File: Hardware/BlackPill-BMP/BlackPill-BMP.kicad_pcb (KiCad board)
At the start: 2 copper layers, 72.4 x 60 mm, 39 parts, among them J1 JTAG, J2 VCC, J3 GND, J4 SWO, J5 GDB_COMM, J6 TVCC, J7 LogicAna, J8 Conn_01x10, J9 Conn_01x11, U1 BlueAndBlackPill, U2 AD8531ARTZ, U3 SRV05-4, U4 TXS0108EPW, U5 SRV05-4

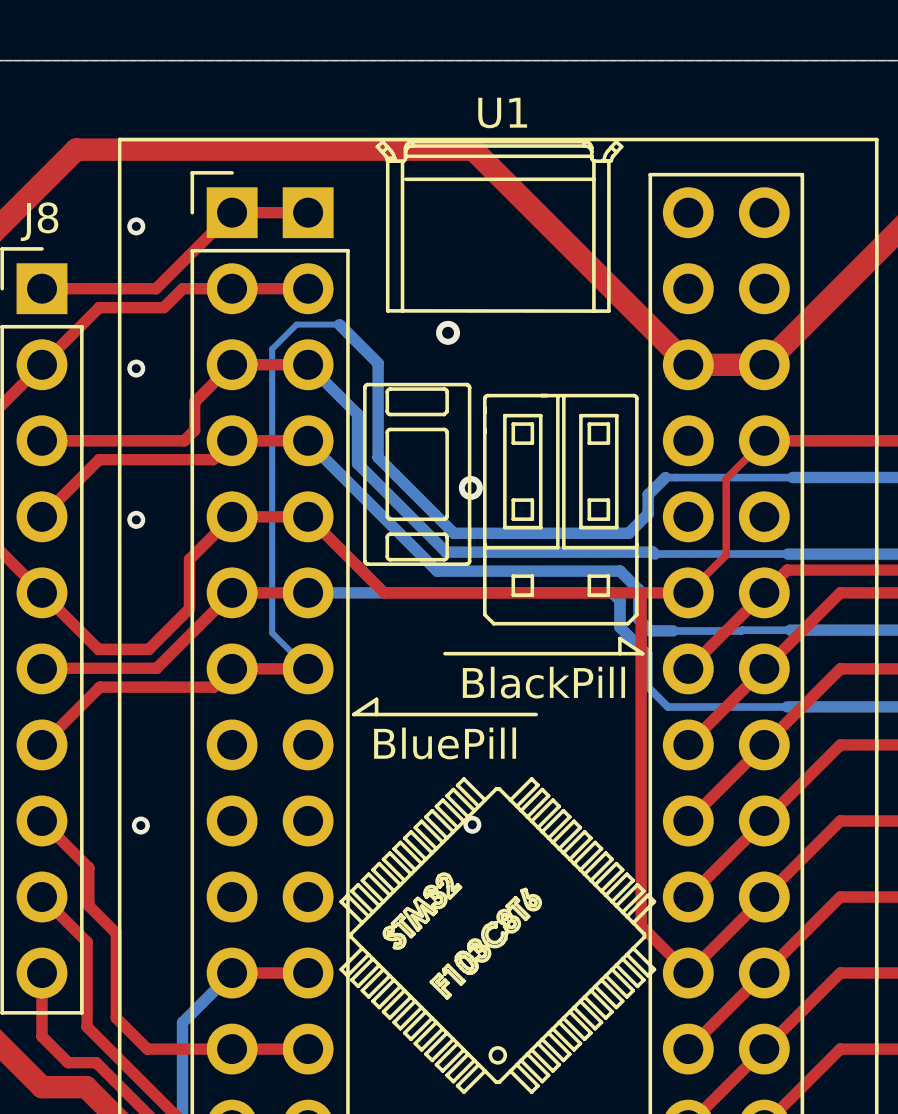
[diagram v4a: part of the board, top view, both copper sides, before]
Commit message: Files for PCB Manufacturing of 4 boards. Preparation for Board documentation
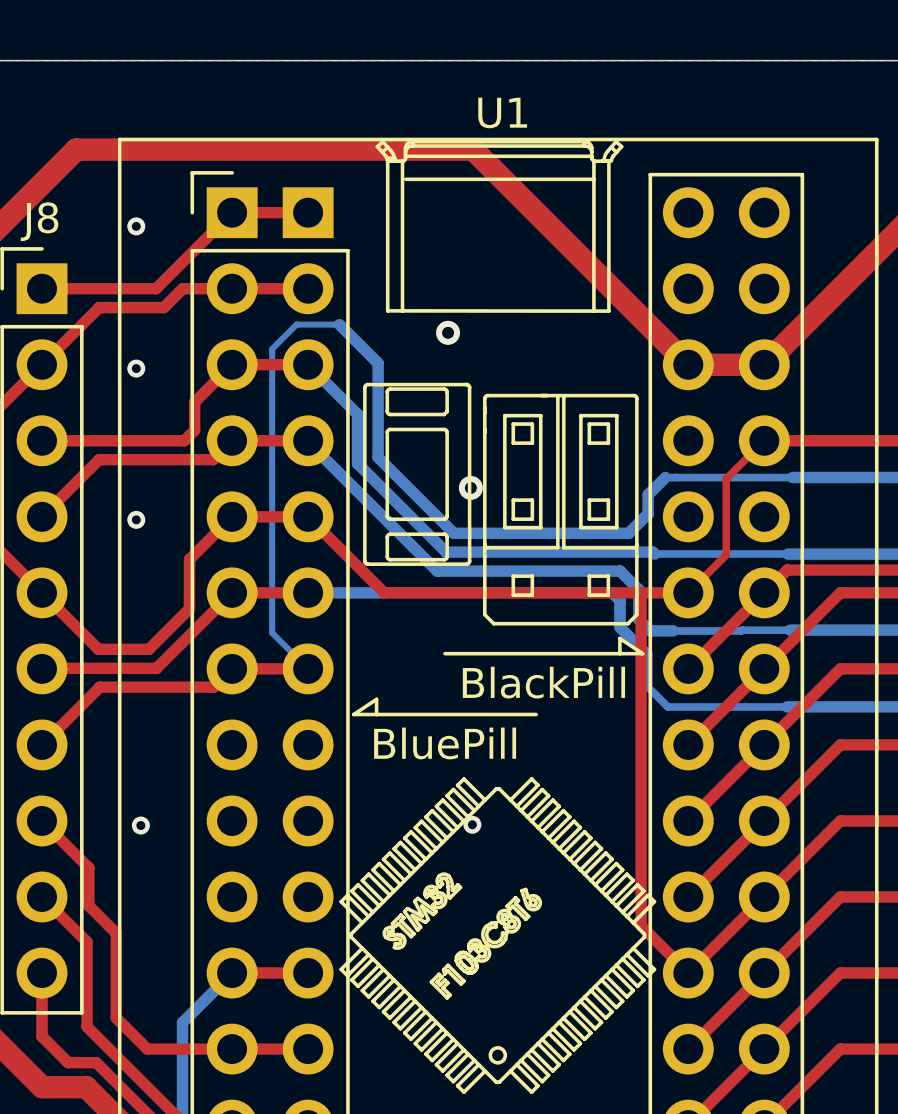
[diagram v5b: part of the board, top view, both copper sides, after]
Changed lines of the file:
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@@
     (fp_arc (start 9.164109 23.475359) (mid 9.19312 23.534447) (end 9.169421 23.59583) (layer "F.SilkS") (width 0.12))
     (fp_arc (start 7.057769 23.137421) (mid 6.881082 23.21257) (end 6.704534 23.137103) (layer "F.SilkS") (width 0.12))
-    (fp_arc (start 5.238052 24.032461) (mid 5.300519 24.004429) (end 5.368722 24.010576) (layer "F.SilkS") (width 0.12))
+    (fp_arc (start 5.238052 24.032461) (mid 5.300525 24.004403) (end 5.368722 24.010576) (layer "F.SilkS") (width 0.12))
     (fp_arc (start 6.919342 22.160794) (mid 7.078414 22.093934) (end 7.23752 22.160688) (layer "F.SilkS") (width 0.12))
     (fp_arc (start 5.698 35.022588) (mid 3.648 32.972588) (end 5.698 30.922588) (layer "F.SilkS") (width 0.12))
@@
     (fp_arc (start 4.534 11.742) (mid 4.463289 11.712711) (end 4.434 11.642) (layer "F.SilkS") (width 0.12))
     (fp_arc (start 5.153056 37.032958) (mid 5.435907 37.150103) (end 5.553056 37.432958) (layer "F.SilkS") (width 0.12))
-    (fp_arc (start 5.139252 24.209874) (mid 5.084094 24.072059) (end 5.143927 23.93621) (layer "F.SilkS") (width 0.12))
+    (fp_arc (start 5.139252 24.209874) (mid 5.084089 24.072059) (end 5.143927 23.93621) (layer "F.SilkS") (width 0.12))
     (fp_arc (start 9.317515 23.529327) (mid 9.430619 23.534642) (end 9.527224 23.593706) (layer "F.SilkS") (width 0.12))
     (fp_arc (start 5.459023 24.262355) (mid 5.542039 24.256717) (end 5.62082 24.283496) (layer "F.SilkS") (width 0.12))
-    (fp_arc (start 8.952381 23.377727) (mid 9.10311 23.311203) (end 9.254729 23.375603) (layer "F.SilkS") (width 0.12))
+    (fp_arc (start 8.952381 23.377727) (mid 9.10311 23.311139) (end 9.254729 23.375603) (layer "F.SilkS") (width 0.12))
     (fp_arc (start 11.765 -2.226605) (mid 11.931822 -2.175277) (end 12.014999 -2.021817) (layer "F.SilkS") (width 0.12))
     (fp_arc (start 5.284 6.742) (mid 5.213289 6.712711) (end 5.184 6.642) (layer "F.SilkS") (width 0.12))
@@
     (fp_arc (start 8.035776 25.146132) (mid 8.038453 25.196504) (end 8.014105 25.240682) (layer "F.SilkS") (width 0.12))
     (fp_arc (start 10.130326 23.124461) (mid 10.057435 23.149835) (end 9.98797 23.116175) (layer "F.SilkS") (width 0.12))
-    (fp_arc (start 4.96647 38.715042) (mid 4.943912 38.616314) (end 4.944082 38.515042) (layer "F.SilkS") (width 0.12))
+    (fp_arc (start 4.96647 38.715042) (mid 4.943897 38.616315) (end 4.944082 38.515042) (layer "F.SilkS") (width 0.12))
     (fp_arc (start 5.131166 -1.890847) (mid 5.176978 -1.815287) (end 5.193572 -1.7285) (layer "F.SilkS") (width 0.12))
     (fp_arc (start 8.519575 24.925586) (mid 8.342887 25.00072) (end 8.166341 24.925267) (layer "F.SilkS") (width 0.12))
@@
     (fp_arc (start 7.23752 22.160688) (mid 7.328273 22.324575) (end 7.354273 22.510098) (layer "F.SilkS") (width 0.12))
     (fp_arc (start 12.859998 39.524619) (mid 12.830711 39.594711) (end 12.760619 39.623998) (layer "F.SilkS") (width 0.12))
-    (fp_arc (start 5.315142 -2.054759) (mid 5.407732 -1.900877) (end 5.439988 -1.724215) (layer "F.SilkS") (width 0.12))
+    (fp_arc (start 5.315142 -2.054759) (mid 5.407707 -1.900875) (end 5.439988 -1.724215) (layer "F.SilkS") (width 0.12))
     (fp_arc (start 8.441283 6.21) (mid 8.470571 6.139283) (end 8.541283 6.11) (layer "F.SilkS") (width 0.12))
     (fp_arc (start 9.265884 23.689744) (mid 9.344175 23.652102) (end 9.425556 23.682413) (layer "F.SilkS") (width 0.12))
@@
       (net 55 "unconnected-(U1-PadB40)") (pinfunction "5V") (pintype "power_in+no_connect"))
     (model "${KIPRJMOD}/lib/blackpill v2.0.step"
-      (offset (xyz 10 -25 5.5))
+      (offset (xyz 10 -25 10))
       (scale (xyz 1 1 1))
       (rotate (xyz 0 0 90))
     )
     (model "${KICAD6_3DMODEL_DIR}/Connector_PinHeader_2.54mm.3dshapes/PinHeader_1x20_P2.54mm_Vertical.wrl"
-      (offset (xyz 2.5 0 5.5))
+      (offset (xyz 2.5 0 10))
       (scale (xyz 1 1 1))
       (rotate (xyz 0 180 0))
     )
     (model "${KICAD6_3DMODEL_DIR}/Connector_PinHeader_2.54mm.3dshapes/PinHeader_1x20_P2.54mm_Vertical.wrl"
-      (offset (xyz 17.6 0 5.5))
+      (offset (xyz 17.6 0 10))
       (scale (xyz 1 1 1))
       (rotate (xyz 0 -180 0))
     )
+    (model "${KICAD6_3DMODEL_DIR}/Connector_PinSocket_2.54mm.3dshapes/PinSocket_2x20_P2.54mm_Vertical.wrl"
+      (offset (xyz 2.5 0 0))
+      (scale (xyz 1 1 1))
+      (rotate (xyz 0 0 0))
+    )
+    (model "${KICAD6_3DMODEL_DIR}/Connector_PinSocket_2.54mm.3dshapes/PinSocket_2x20_P2.54mm_Vertical.wrl"
+      (offset (xyz 17.8 0 0))
+      (scale (xyz 1 1 1))
+      (rotate (xyz 0 0 0))
+    )
+    (model "P:/github.com/glossy-msp430/Hardware/BluePill-BMP/lib/YAAJ_BluePill_PinHeaders_H_SWD_cp.wrl" hide
+      (offset (xyz 0 0 7.5))
+      (scale (xyz 1 1 1))
+      (rotate (xyz 0 0 0))
+    )
   )

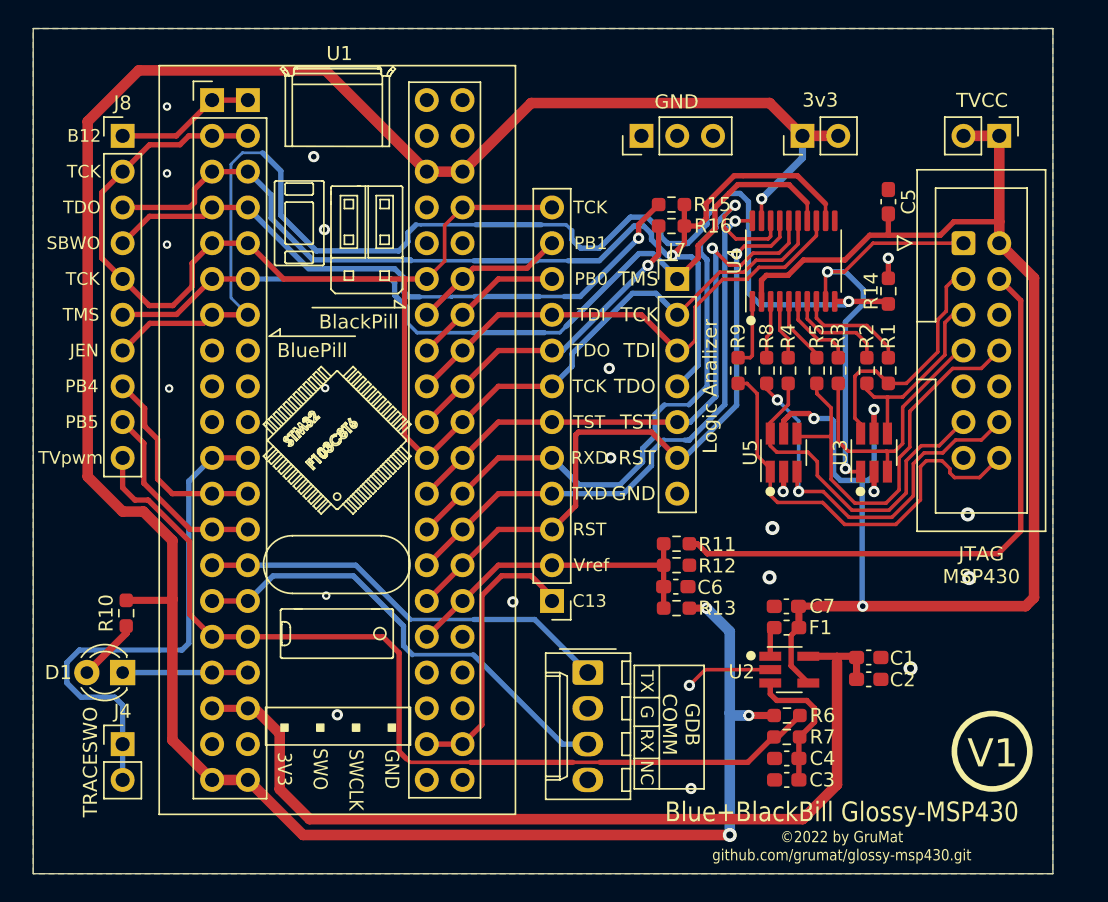
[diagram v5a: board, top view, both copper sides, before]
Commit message: Swapped LRXD and LTXD on both prototype boards.
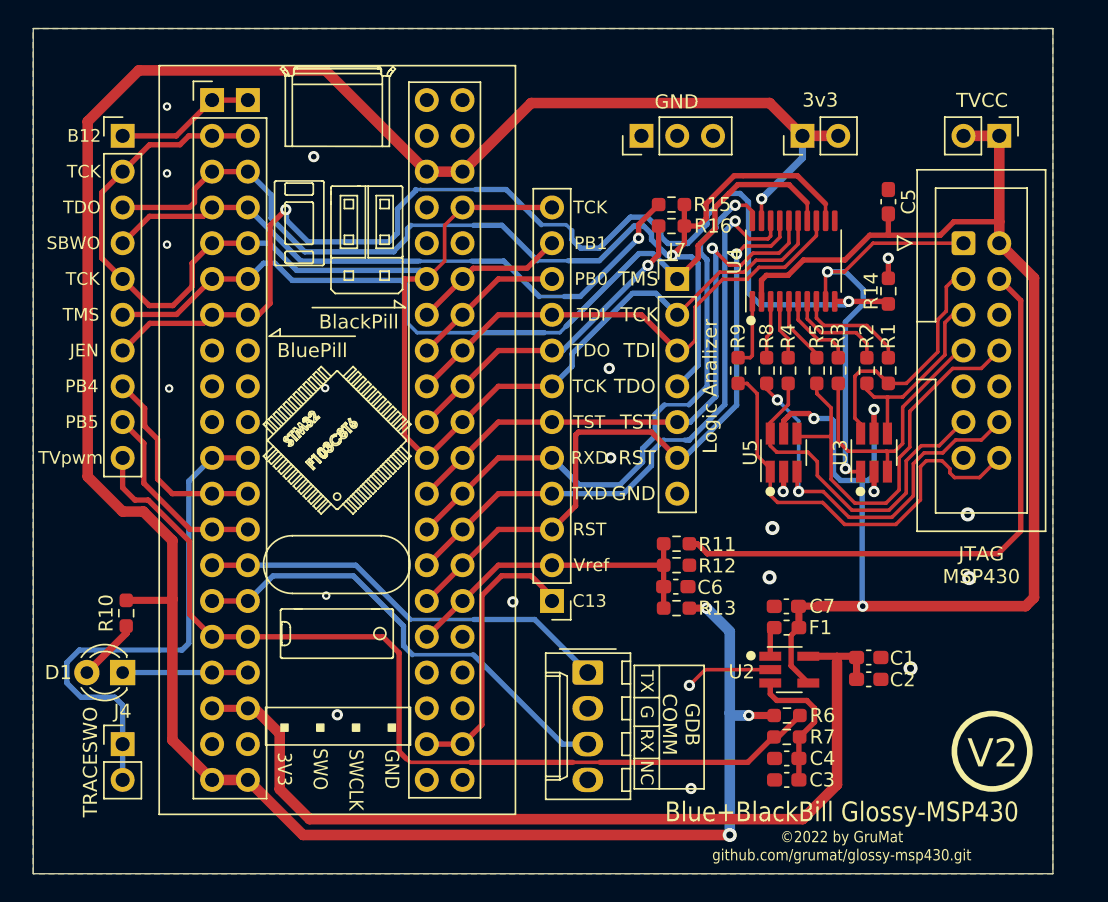
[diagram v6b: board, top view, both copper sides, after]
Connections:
- R8 pad 1: /LRXD -> /LTXD
- R9 pad 1: /LTXD -> /LRXD
- U4 pad 1: /LTXD -> /LRXD
- U4 pad 18: /mRXD -> /mTXD
- U4 pad 20: /mTXD -> /mRXD
- U4 pad 3: /LRXD -> /LTXD
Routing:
- net /JENA: track 87.1 -> 79.8 mm, vias 1 -> 2
- net /mRXD: track 50.8 -> 46.2 mm
- net /mTXD: track 41.0 -> 44.2 mm
- net /LTDO: track 75.8 -> 77.8 mm
- net /mTCK: track 106.9 -> 108.6 mm
- net /mTMS: track 68.8 -> 70.1 mm
- net /LTXD: track 4.92 -> 4.11 mm
- net /LRXD: track 4.11 -> 4.92 mm
- net /SBWO: track 45.6 -> 45.0 mm
- net GND: vias 22 -> 21
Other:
- board text added: "V2"
- board text removed: "V1"

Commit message: Review of ESD protection for Development boards.
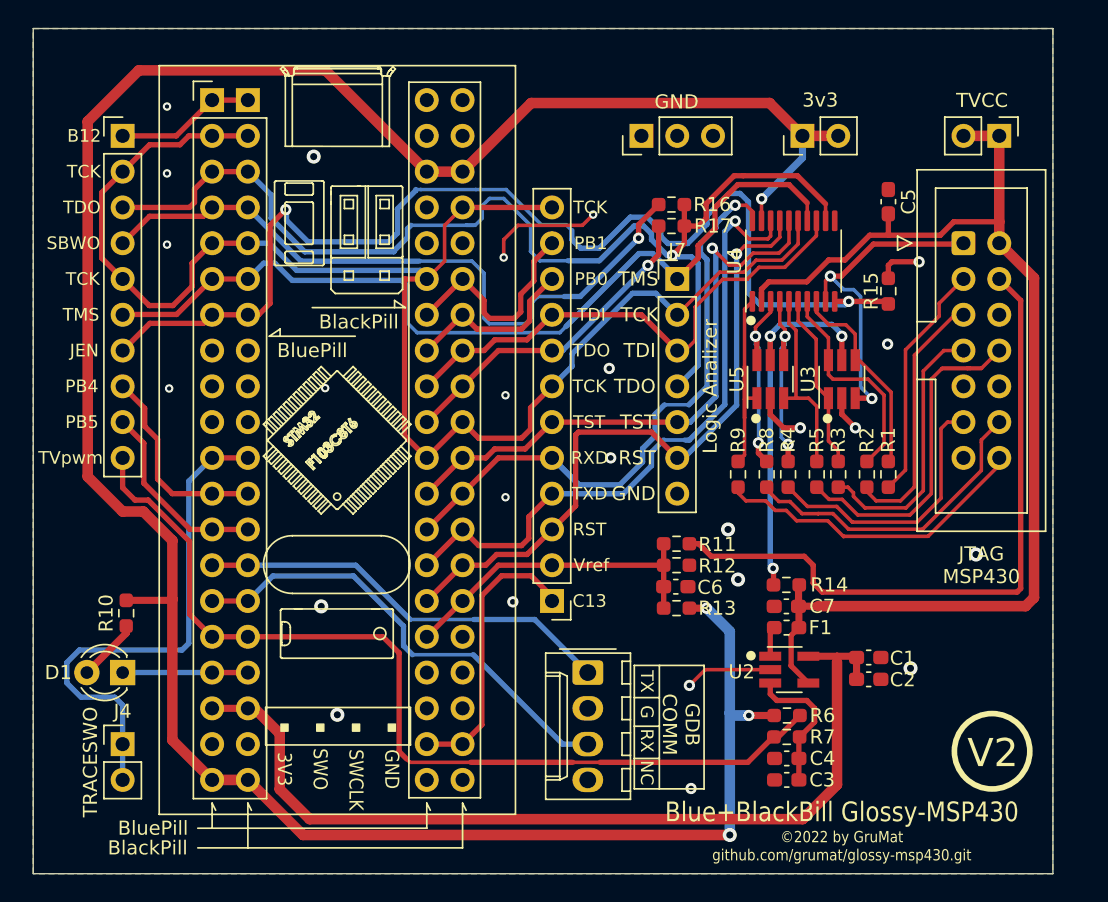
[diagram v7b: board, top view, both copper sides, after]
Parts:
- added R14: 10K, Resistor_SMD:R_0603_1608Metric_Pad0.98x0.95mm_HandSolder, F.Cu at (170.3, 104.5)
- R8, R9: value 100 -> 330
- moved R1 7.37 mm to (177.5, 96.6)
- moved R2 7.37 mm to (176.0, 96.6)
- moved R3 7.37 mm to (174.0, 96.6)
- moved R4 7.37 mm to (170.4, 96.6)
- moved R5 7.37 mm to (172.5, 96.6)
- moved R8 7.37 mm to (168.9, 96.6)
- moved R9 7.37 mm to (166.9, 96.6)
- moved U3 5.69 mm to (174.2, 89.9)
- moved U5 5.30 mm to (169.2, 89.9)
- renumbered R14 to R15, R15 to R16, R16 to R17
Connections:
- U3 pad 1: /JTDO -> /LTCK
- U3 pad 3: /JTCK -> /JTDO
- U3 pad 4: /JTMS -> /LTDI
- U3 pad 5: /TVCC -> Net-(R14-Pad2)
- U3 pad 6: /JTDI -> /LTMS
- U5 pad 1: /JRXD -> /LRXD
- U5 pad 3: /JTXD -> /LTEST
- U5 pad 4: /JTEST -> /LRST
- U5 pad 5: /TVCC -> Net-(R14-Pad2)
- U5 pad 6: /JRST -> /LTXD
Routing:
- net Net-(R14-Pad2): track 0.00 -> 27.1 mm, vias 0 -> 3
- net /TVCC: track 108.3 -> 82.3 mm, vias 3 -> 0
- net GND: track 10.5 -> 24.0 mm, vias 21 -> 25
- net /LRXD: track 4.92 -> 16.3 mm
- net /LTXD: track 4.11 -> 13.9 mm, vias 0 -> 2
- net /LRST: track 4.24 -> 13.6 mm, vias 0 -> 2
- net /LTEST: track 4.81 -> 13.6 mm
- net /LTMS: track 7.21 -> 15.6 mm
- net /JRXD: track 30.9 -> 22.9 mm
- net /JTXD: track 29.2 -> 22.2 mm, vias 2 -> 0
- net /LTCK: track 5.71 -> 12.5 mm
- net /LTDI: track 7.90 -> 14.5 mm
- net /JTDO: track 30.1 -> 23.9 mm
- net /JRST: track 25.1 -> 19.3 mm
- net /TVref: track 43.0 -> 48.4 mm
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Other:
- board text added: "BlackPill"
- board text added: "BluePill"

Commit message: Swap mTMS and JENA pins for optimized DMA use in BluePill variant.
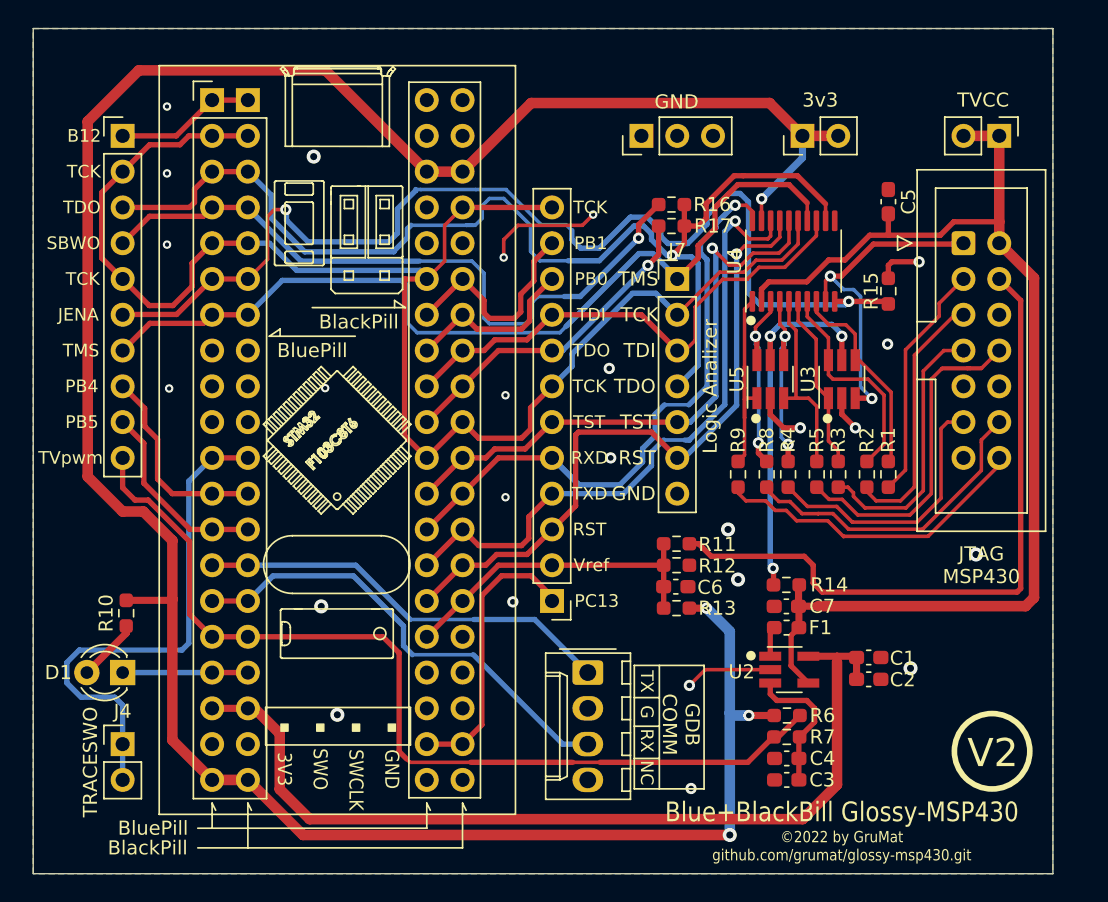
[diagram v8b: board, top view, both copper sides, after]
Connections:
- J8 pad 6: /mTMS -> /JENA
- J8 pad 7: /JENA -> /mTMS
- U1 pad A6: /mTMS -> /JENA
- U1 pad A7: /JENA -> /mTMS
- U1 pad B6: /mTMS -> /JENA
- U1 pad B7: /JENA -> /mTMS
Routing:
- net /JENA: track 79.8 -> 77.3 mm
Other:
- board text added: "JENA"
- board text added: "PC13"
- board text added: "TVCC"
- board text removed: "C13"
- board text removed: "JEN"
